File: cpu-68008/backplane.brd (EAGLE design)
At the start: 99.7 x 99.7 mm, 45 parts, among them IC101 74HCT245, IC102 74HCT245, IC103 74HCT245, IC104 74HCT245, IC201 GAL22V10D

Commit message: added r/w and reset to backplane; fixed some missing mouser p/n on cpu board
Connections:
- removed net N$12: IC201.8
- new net !SLOT_RESET: IC104.11, IC201.8, SV301.30, SV302.30, SV303.30, SV304.30
- net !RESET: now also IC104.9
- net SLOT_R/!W!: now also SV301.23, SV302.23, SV303.23, SV304.23
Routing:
- net !SLOT_RESET: track 0.00 -> 134.5 mm, vias 0 -> 3
- net SLOT_R/!W!: track 63.0 -> 129.3 mm
- net !RESET: track 12.0 -> 23.7 mm, vias 0 -> 1
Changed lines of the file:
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@@
 <wire x1="63.5" y1="88.3971" x2="60.4571" y2="91.44" width="0.2032" layer="16"/>
 <wire x1="60.4571" y1="91.44" x2="58.42" y2="91.44" width="0.2032" layer="16"/>
+<contactref element="IC104" pad="9"/>
+<wire x1="64.77" y1="85.09" x2="66.04" y2="83.82" width="0.2032" layer="16"/>
+<via x="70.485" y="81.7428" extent="1-16" drill="0.35"/>
+<wire x1="68.4078" y1="83.82" x2="69.9036" y2="82.3242" width="0.2032" layer="16"/>
+<wire x1="69.9036" y1="82.3242" x2="69.9036" y2="82.309175" width="0.2032" layer="16"/>
+<wire x1="69.9036" y1="82.309175" x2="70.244175" y2="81.9686" width="0.2032" layer="16"/>
+<wire x1="70.244175" y1="81.9686" x2="70.2592" y2="81.9686" width="0.2032" layer="16"/>
+<wire x1="70.2592" y1="81.9686" x2="70.485" y2="81.7428" width="0.2032" layer="16"/>
+<wire x1="70.485" y1="81.7428" x2="71.12" y2="81.1078" width="0.2032" layer="1"/>
+<wire x1="71.12" y1="81.1078" x2="71.12" y2="77.4192" width="0.2032" layer="1"/>
+<wire x1="66.04" y1="83.82" x2="68.4078" y2="83.82" width="0.2032" layer="16"/>
 </signal>
 <signal name="!AS">
@@
 <wire x1="74.93" y1="72.39" x2="21.59" y2="72.39" width="0.2032" layer="16"/>
 <wire x1="21.59" y1="72.39" x2="19.685" y2="74.295" width="0.2032" layer="16"/>
-</signal>
-<signal name="N$12">
-<contactref element="IC201" pad="8"/>
+<contactref element="SV302" pad="23"/>
+<contactref element="SV304" pad="23"/>
+<contactref element="SV303" pad="23"/>
+<contactref element="SV301" pad="23"/>
+<wire x1="74.93" y1="67.3608" x2="74.93" y2="64.77" width="0.2032" layer="1"/>
+<wire x1="66.675" y1="56.515" x2="66.675" y2="55.245" width="0.2032" layer="1"/>
+<wire x1="74.93" y1="64.77" x2="66.675" y2="56.515" width="0.2032" layer="1"/>
+<wire x1="66.675" y1="55.245" x2="67.945" y2="53.975" width="0.2032" layer="16"/>
+<wire x1="67.945" y1="40.64" x2="66.675" y2="39.37" width="0.2032" layer="16"/>
+<wire x1="67.945" y1="53.975" x2="67.945" y2="40.64" width="0.2032" layer="16"/>
+<wire x1="66.675" y1="39.37" x2="67.945" y2="38.1" width="0.2032" layer="16"/>
+<wire x1="67.945" y1="38.1" x2="67.945" y2="24.765" width="0.2032" layer="16"/>
+<wire x1="67.945" y1="24.765" x2="66.675" y2="23.495" width="0.2032" layer="16"/>
+<wire x1="66.675" y1="23.495" x2="67.945" y2="22.225" width="0.2032" layer="16"/>
+<wire x1="67.945" y1="22.225" x2="67.945" y2="8.89" width="0.2032" layer="16"/>
+<wire x1="67.945" y1="8.89" x2="66.675" y2="7.62" width="0.2032" layer="16"/>
 </signal>
 <signal name="N$13">
@@
 <via x="18.415" y="49.53" extent="1-16" drill="0.35"/>
 </signal>
+<signal name="!SLOT_RESET">
+<contactref element="SV302" pad="30"/>
+<contactref element="SV304" pad="30"/>
+<contactref element="SV303" pad="30"/>
+<contactref element="SV301" pad="30"/>
+<contactref element="IC201" pad="8"/>
+<contactref element="IC104" pad="11"/>
+<wire x1="69.85" y1="67.3608" x2="69.85" y2="60.96" width="0.2032" layer="1"/>
+<via x="69.85" y="60.96" extent="1-16" drill="0.35"/>
+<wire x1="69.85" y1="60.96" x2="73.025" y2="57.785" width="0.2032" layer="16"/>
+<wire x1="73.025" y1="53.34" x2="73.66" y2="52.705" width="0.2032" layer="16"/>
+<wire x1="73.66" y1="52.705" x2="74.295" y2="52.705" width="0.2032" layer="16"/>
+<wire x1="73.025" y1="57.785" x2="73.025" y2="53.34" width="0.2032" layer="16"/>
+<wire x1="74.295" y1="50.987225" x2="74.295" y2="52.705" width="0.2032" layer="16"/>
+<wire x1="74.295" y1="36.83" x2="74.2" y2="36.83" width="0.2032" layer="16"/>
+<wire x1="74.295" y1="36.83" x2="73.025" y2="35.56" width="0.2032" layer="16"/>
+<wire x1="73.025" y1="35.56" x2="73.025" y2="22.225" width="0.2032" layer="16"/>
+<wire x1="73.025" y1="22.225" x2="74.295" y2="20.955" width="0.2032" layer="16"/>
+<wire x1="74.295" y1="20.955" x2="73.025" y2="19.685" width="0.2032" layer="16"/>
+<wire x1="73.025" y1="19.685" x2="73.025" y2="6.35" width="0.2032" layer="16"/>
+<wire x1="73.025" y1="6.35" x2="74.295" y2="5.08" width="0.2032" layer="16"/>
+<wire x1="74.295" y1="36.83" x2="73.025" y2="38.1" width="0.2032" layer="16"/>
+<wire x1="73.025" y1="38.1" x2="73.025" y2="49.717225" width="0.2032" layer="16"/>
+<wire x1="73.025" y1="49.717225" x2="74.295" y2="50.987225" width="0.2032" layer="16"/>
+<wire x1="14.605" y1="73.66" x2="15.875" y2="72.39" width="0.2032" layer="16"/>
+<via x="15.875" y="72.39" extent="1-16" drill="0.35"/>
+<wire x1="15.875" y1="66.04" x2="17.145" y2="64.77" width="0.2032" layer="1"/>
+<via x="17.145" y="64.77" extent="1-16" drill="0.35"/>
+<wire x1="17.145" y1="64.77" x2="64.77" y2="64.77" width="0.2032" layer="16"/>
+<wire x1="64.77" y1="64.77" x2="68.58" y2="60.96" width="0.2032" layer="16"/>
+<wire x1="68.58" y1="60.96" x2="69.85" y2="60.96" width="0.2032" layer="16"/>
+<wire x1="14.605" y1="76.2" x2="14.605" y2="73.66" width="0.2032" layer="16"/>
+<wire x1="15.875" y1="72.39" x2="15.875" y2="66.04" width="0.2032" layer="1"/>
+</signal>
 </signals>

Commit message: added /DS to GALs on all peripherals and backplane began work on TMS9918 video card
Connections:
- removed net N$13: IC201.9
- net !SLOT_DS: now also IC201.9
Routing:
- net !SLOT_DS: track 62.4 -> 135.0 mm, vias 0 -> 3
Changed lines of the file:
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@@
 <wire x1="13.97" y1="95.25" x2="13.97" y2="92.71" width="0.8128" layer="16"/>
 <wire x1="21.59" y1="87.63" x2="21.59" y2="85.09" width="0.8128" layer="16"/>
-<wire x1="13.9065" y1="95.3135" x2="13.97" y2="95.25" width="0.8128" layer="16"/>
 <wire x1="49.53" y1="69.215" x2="33.02" y2="69.215" width="0.4064" layer="16"/>
 <wire x1="33.02" y1="69.215" x2="32.385" y2="68.58" width="0.4064" layer="16"/>
@@
 <wire x1="67.945" y1="8.89" x2="66.675" y2="7.62" width="0.2032" layer="16"/>
 </signal>
-<signal name="N$13">
-<contactref element="IC201" pad="9"/>
-</signal>
 <signal name="N$14">
 <contactref element="IC201" pad="10"/>
@@
 <wire x1="76.835" y1="22.6329" x2="77.8002" y2="21.6677" width="0.2032" layer="16"/>
 <wire x1="77.8002" y1="21.6677" x2="77.8002" y2="19.2852" width="0.2032" layer="16"/>
+<contactref element="IC201" pad="9"/>
+<wire x1="77.47" y1="67.3608" x2="77.47" y2="70.485" width="0.2032" layer="1"/>
+<via x="77.47" y="70.485" extent="1-16" drill="0.35"/>
+<wire x1="77.47" y1="70.485" x2="76.835" y2="70.485" width="0.2032" layer="16"/>
+<wire x1="76.835" y1="70.485" x2="76.2" y2="69.85" width="0.2032" layer="16"/>
+<wire x1="76.2" y1="69.85" x2="68.9467125" y2="69.85" width="0.2032" layer="16"/>
+<wire x1="68.9467125" y1="69.85" x2="68.9327125" y2="69.864" width="0.2032" layer="16"/>
+<wire x1="68.9327125" y1="69.864" x2="66.3222875" y2="69.864" width="0.2032" layer="16"/>
+<wire x1="66.3222875" y1="69.864" x2="66.3082875" y2="69.85" width="0.2032" layer="16"/>
+<wire x1="34.338" y1="69.85" x2="34.29" y2="69.898" width="0.2032" layer="16"/>
+<via x="34.29" y="69.898" extent="1-16" drill="0.35"/>
+<wire x1="34.29" y1="69.898" x2="30.528" y2="73.66" width="0.2032" layer="1"/>
+<via x="13.335" y="73.66" extent="1-16" drill="0.35"/>
+<wire x1="13.335" y1="73.66" x2="12.7" y2="73.66" width="0.2032" layer="16"/>
+<wire x1="12.7" y1="73.66" x2="12.065" y2="74.295" width="0.2032" layer="16"/>
+<wire x1="12.065" y1="74.295" x2="12.065" y2="76.2" width="0.2032" layer="16"/>
+<wire x1="66.3082875" y1="69.85" x2="34.338" y2="69.85" width="0.2032" layer="16"/>
+<wire x1="30.528" y1="73.66" x2="13.335" y2="73.66" width="0.2032" layer="1"/>
 </signal>
 <signal name="SLOT_A8">
@@
 <contactref element="LED303" pad="A"/>
 <wire x1="16.725" y1="22.225" x2="19.84" y2="22.225" width="0.2032" layer="1"/>
-<wire x1="20.32" y1="22.225" x2="19.84" y2="22.225" width="0.2032" layer="1"/>
 </signal>
 <signal name="!SLOT_ACK">
@@
 <wire x1="73.025" y1="57.785" x2="73.025" y2="53.34" width="0.2032" layer="16"/>
 <wire x1="74.295" y1="50.987225" x2="74.295" y2="52.705" width="0.2032" layer="16"/>
-<wire x1="74.295" y1="36.83" x2="74.2" y2="36.83" width="0.2032" layer="16"/>
 <wire x1="74.295" y1="36.83" x2="73.025" y2="35.56" width="0.2032" layer="16"/>
 <wire x1="73.025" y1="35.56" x2="73.025" y2="22.225" width="0.2032" layer="16"/>

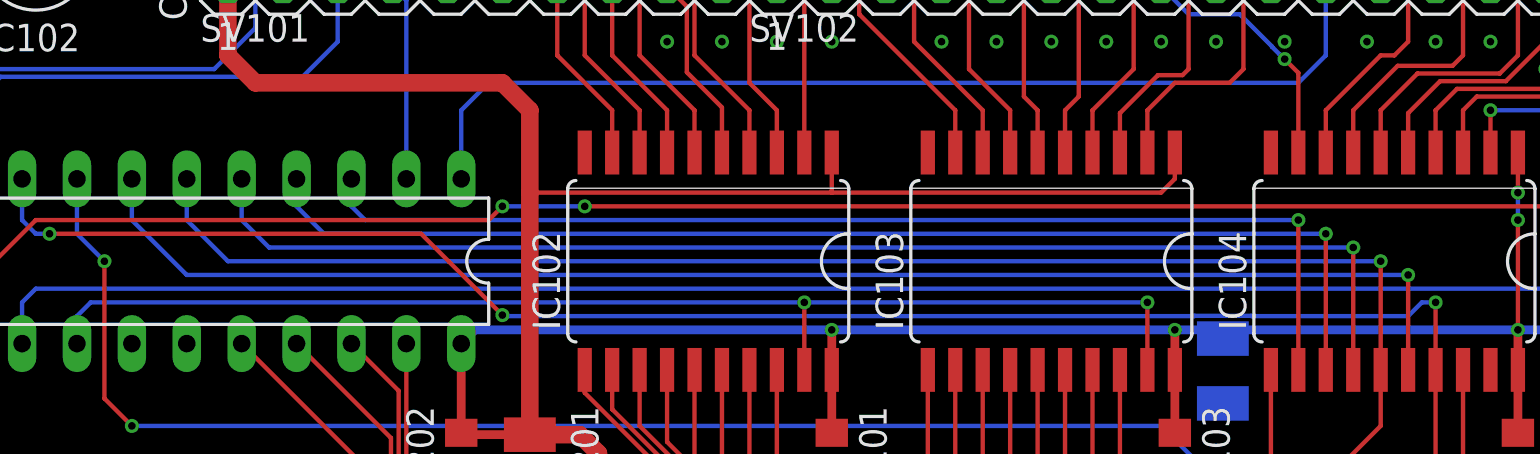
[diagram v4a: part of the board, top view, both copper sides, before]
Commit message: finished schematic for tms9918 board, started routing
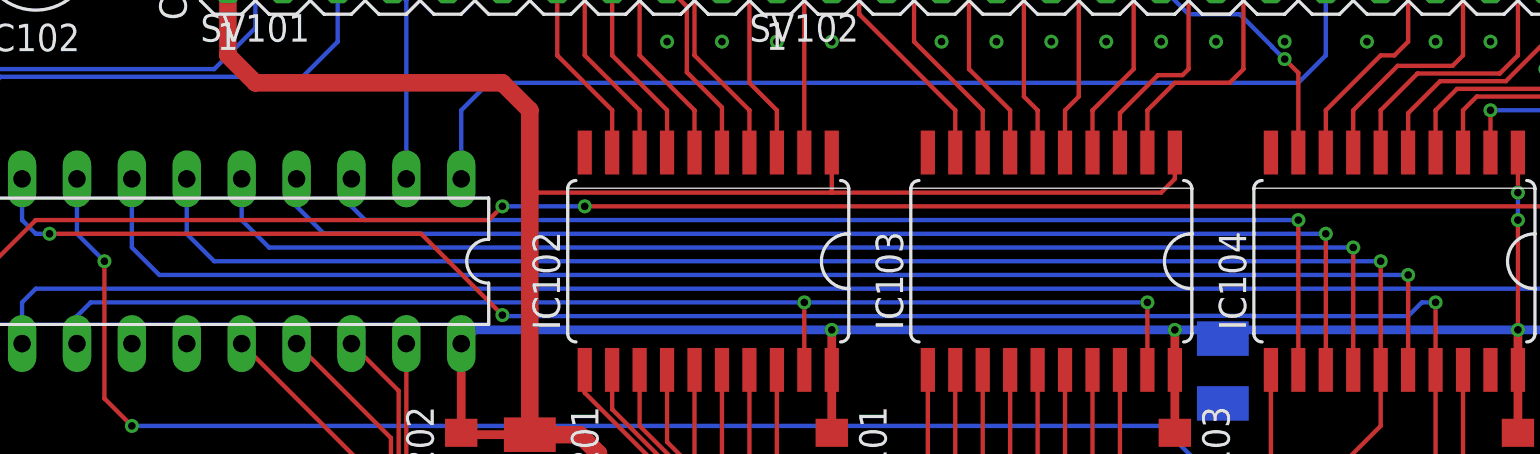
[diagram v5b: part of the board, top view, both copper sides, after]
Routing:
- net SLOT_A19: track 66.4 -> 67.2 mm
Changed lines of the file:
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@@
 <wire x1="76.2" y1="67.3608" x2="76.2" y2="71.755" width="0.2032" layer="1"/>
 <via x="76.2" y="71.755" extent="1-16" drill="0.35"/>
-<wire x1="19.685" y1="71.755" x2="17.145" y2="74.295" width="0.2032" layer="16"/>
-<wire x1="17.145" y1="74.295" x2="17.145" y2="76.2" width="0.2032" layer="16"/>
-<wire x1="76.2" y1="71.755" x2="19.685" y2="71.755" width="0.2032" layer="16"/>
+<wire x1="18.415" y1="71.755" x2="17.145" y2="73.025" width="0.2032" layer="16"/>
+<wire x1="17.145" y1="73.025" x2="17.145" y2="76.2" width="0.2032" layer="16"/>
+<wire x1="76.2" y1="71.755" x2="18.415" y2="71.755" width="0.2032" layer="16"/>
 </signal>
 <signal name="SLOT_R/!W!">
 <contactref element="IC104" pad="15"/>
 <contactref element="IC201" pad="6"/>
-<wire x1="19.685" y1="74.295" x2="19.685" y2="76.2" width="0.2032" layer="16"/>
+<wire x1="19.685" y1="73.66" x2="19.685" y2="76.2" width="0.2032" layer="16"/>
 <wire x1="74.93" y1="67.3608" x2="74.93" y2="72.39" width="0.2032" layer="1"/>
 <via x="74.93" y="72.39" extent="1-16" drill="0.35"/>
-<wire x1="74.93" y1="72.39" x2="21.59" y2="72.39" width="0.2032" layer="16"/>
-<wire x1="21.59" y1="72.39" x2="19.685" y2="74.295" width="0.2032" layer="16"/>
+<wire x1="74.93" y1="72.39" x2="20.955" y2="72.39" width="0.2032" layer="16"/>
+<wire x1="20.955" y1="72.39" x2="19.685" y2="73.66" width="0.2032" layer="16"/>
 <contactref element="SV302" pad="23"/>
 <contactref element="SV304" pad="23"/>

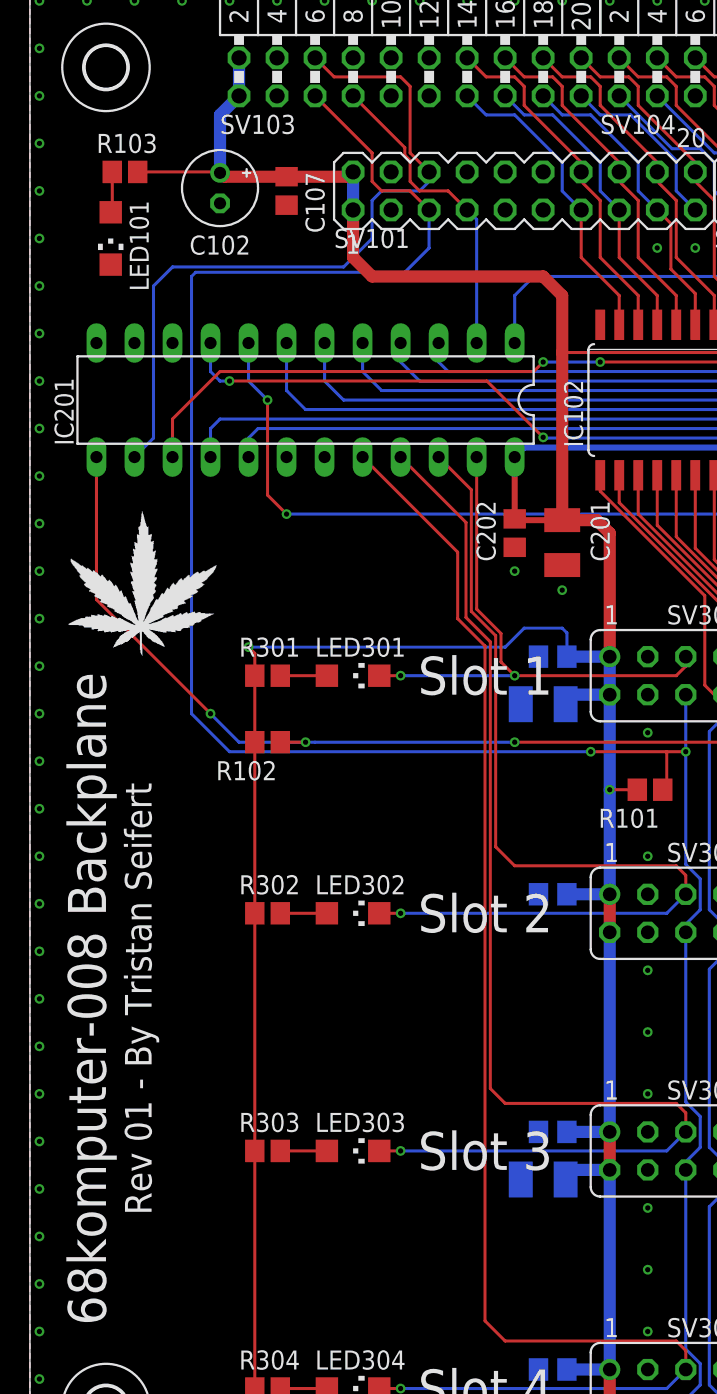
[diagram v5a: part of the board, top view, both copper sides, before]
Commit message: minor revisions on mouser parts
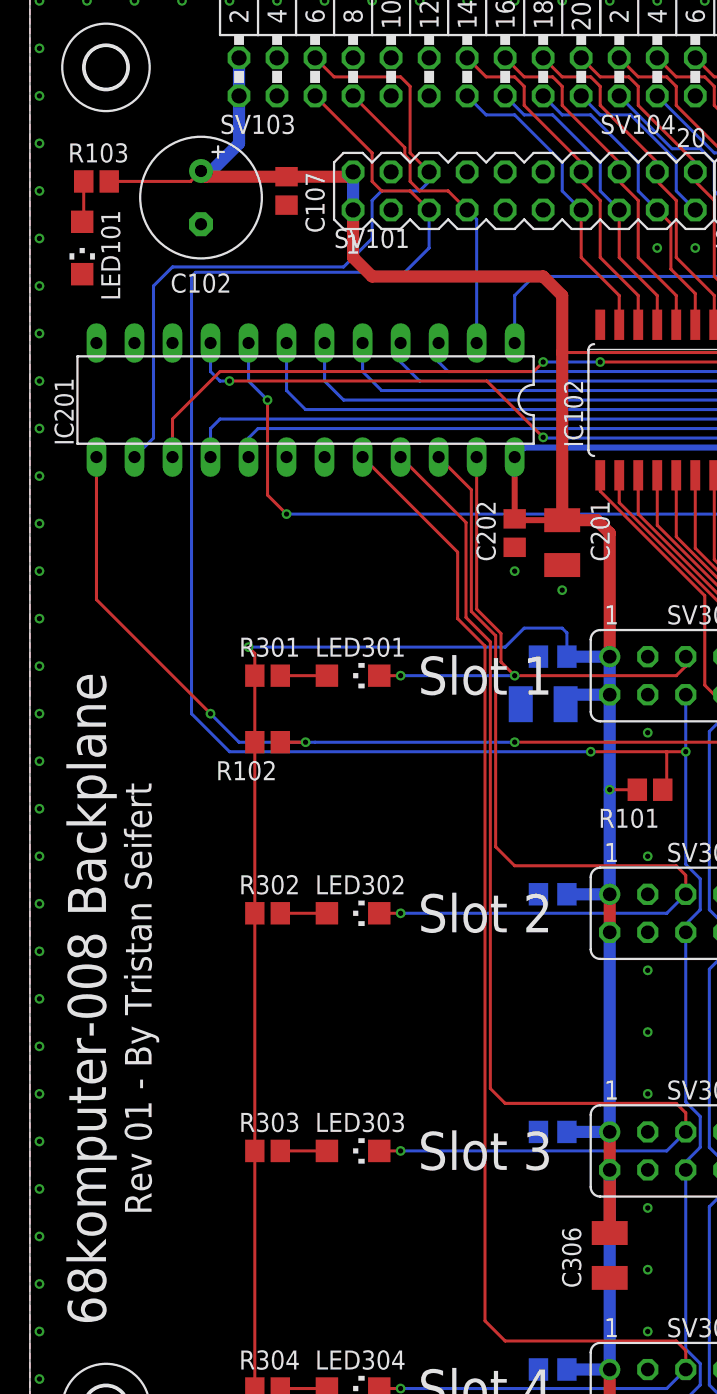
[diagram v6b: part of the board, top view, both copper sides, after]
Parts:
- C102: value 47µF -> 220µF; device rcl:E2-5 -> rcl:E3,5-8
- R301, R302, R303, R304: value 3k -> 1k
- moved WEED301 96.2 mm to (97.8, 41.9), flipped to the bottom
- moved C306 6.75 mm to (38.7, 15.2), flipped to the top, turned to 270 degrees
- moved LED101 2.01 mm to (3.49, 82.5)
- moved R103 2.01 mm to (4.45, 87.0)
- moved C102 1.42 mm to (11.4, 85.9)
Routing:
- net +5V: track 347.3 -> 351.2 mm
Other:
- board text added: "blraaz it"
